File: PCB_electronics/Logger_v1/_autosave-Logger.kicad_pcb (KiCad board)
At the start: 2 copper layers, 87.5 x 52.5 mm, 26 parts, among them P1 GPS_breakout_connector, P10 CONN_01X03, P11 CONN_01X02, P12 CONN_01X02, P13 CONN_01X02, P14 CONN_01X02, P15 CONN_01X02, P2 SD_breakout_connector, P3 Iridium_connector, P4 VN100_connector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

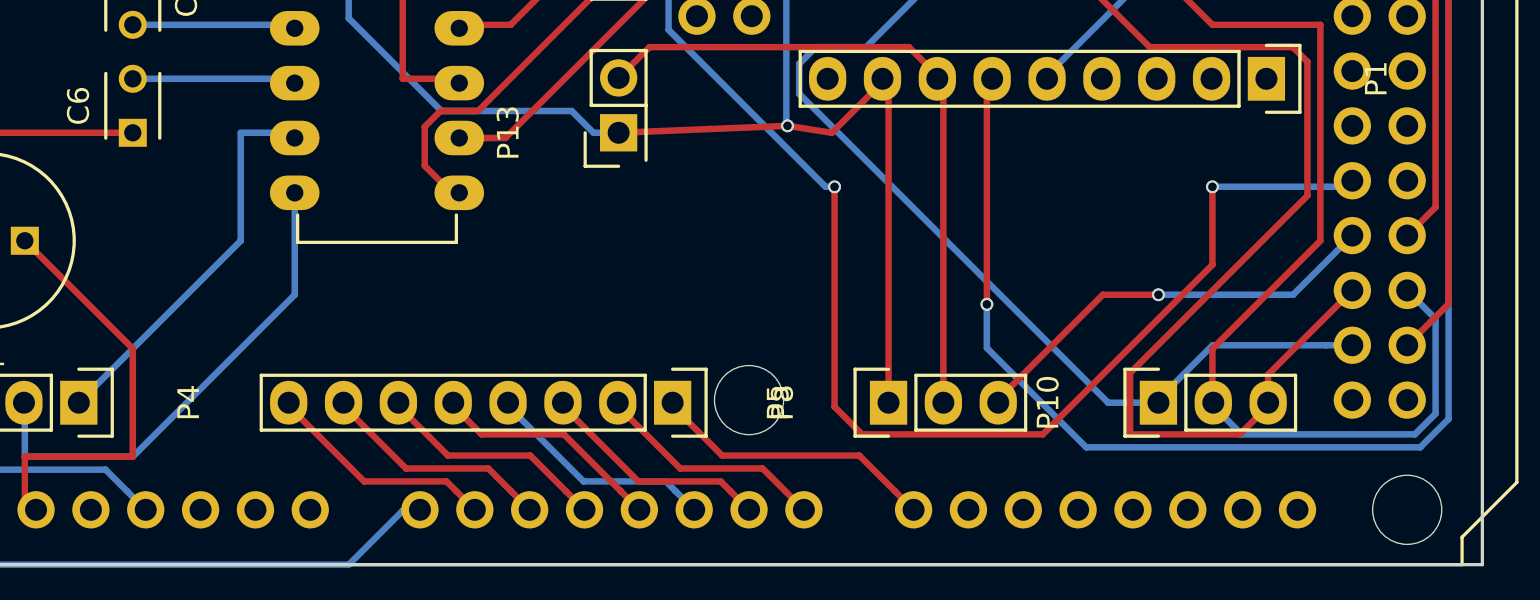
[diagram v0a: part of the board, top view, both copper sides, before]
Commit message: wired board ok
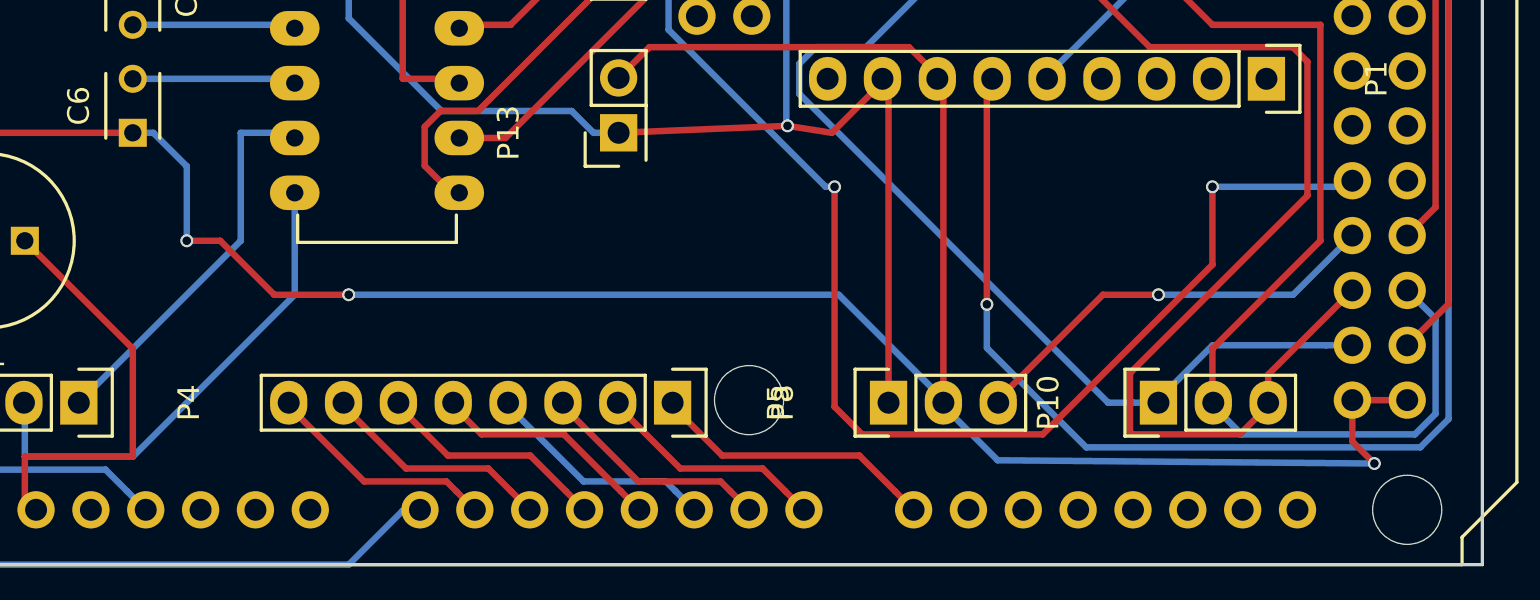
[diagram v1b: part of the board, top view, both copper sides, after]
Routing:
- net GND: track 194.6 -> 266.5 mm, vias 2 -> 5
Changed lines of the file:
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@@
   (general
     (links 82)
-    (no_connects 17)
-    (area 105 82.5 215 142.5)
+    (no_connects 0)
+    (area 124.924999 87.424999 212.575001 140.075001)
     (thickness 1.6)
     (drawings 4)
-    (tracks 353)
+    (tracks 371)
     (zones 0)
     (modules 26)
@@
   (page A4)
   (layers
-    (0 F.Cu signal hide)
-    (31 B.Cu signal hide)
+    (0 F.Cu signal)
+    (31 B.Cu signal)
     (32 B.Adhes user)
     (33 F.Adhes user)
@@
   (gr_line (start 212.5 87.5) (end 212.5 140) (angle 90) (layer Edge.Cuts) (width 0.15))
   (gr_line (start 125 87.5) (end 212.5 87.5) (angle 90) (layer Edge.Cuts) (width 0.15))
+  (segment (start 190.053629 135.166029) (end 207.5 135.31603) (width 0.3) (layer B.Cu) (net 49))
+  (segment (start 206.48 132.38) (end 206.48 134.29603) (width 0.3) (layer F.Cu) (net 49))
+  (segment (start 206.48 134.29603) (end 207.5 135.31603) (width 0.3) (layer F.Cu) (net 49))
+  (via (at 207.5 135.31603) (size 0.6) (drill 0.4) (layers F.Cu B.Cu) (net 49))
+  (segment (start 206.48 132.38) (end 209.02 132.38) (width 0.3) (layer F.Cu) (net 49))
+  (segment (start 187.54 132.5) (end 187.54 132.6524) (width 0.3) (layer B.Cu) (net 49))
+  (segment (start 187.54 132.6524) (end 190.053629 135.166029) (width 0.3) (layer B.Cu) (net 49))
+  (segment (start 152.5 125) (end 152.5 121.55) (width 0.3) (layer B.Cu) (net 49))
+  (segment (start 152.5 121.55) (end 150.95 120) (width 0.3) (layer B.Cu) (net 49))
+  (segment (start 150.95 120) (end 150 120) (width 0.3) (layer B.Cu) (net 49))
+  (segment (start 160 127.5) (end 156.55 127.5) (width 0.3) (layer F.Cu) (net 49))
+  (segment (start 154.05 125) (end 152.5 125) (width 0.3) (layer F.Cu) (net 49))
+  (segment (start 156.55 127.5) (end 154.05 125) (width 0.3) (layer F.Cu) (net 49))
+  (via (at 152.5 125) (size 0.6) (drill 0.4) (layers F.Cu B.Cu) (net 49))
+  (segment (start 187.54 132.5) (end 187.54 132.3476) (width 0.3) (layer B.Cu) (net 49))
+  (segment (start 187.54 132.3476) (end 182.6924 127.5) (width 0.3) (layer B.Cu) (net 49))
+  (segment (start 182.6924 127.5) (end 160 127.5) (width 0.3) (layer B.Cu) (net 49))
+  (via (at 160 127.5) (size 0.6) (drill 0.4) (layers F.Cu B.Cu) (net 49))
   (segment (start 189.88 95) (end 189.88 94.8476) (width 0.3) (layer B.Cu) (net 49))
   (segment (start 139.779599 90.063599) (end 138.916 89.2) (width 0.3) (layer B.Cu) (net 49))
